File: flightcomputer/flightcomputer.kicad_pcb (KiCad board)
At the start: 4 copper layers, 100 x 75 mm, 65 parts, among them J1 Conn_Coaxial, J10 Conn_01x03, J11 Conn_01x03, J12 ESQ-113-14-G-D, J14 S3B-PH-K-S-GW, J2 Conn_Coaxial, J3 Conn_Coaxial, J4 Conn_Coaxial, J5 S3B-PH-K-S-GW, J6 Conn_01x03, J7 S4B-PH-K-S_LF__SN_, J8 Conn_01x03, J9 Conn_01x06, U1 MAX-M10S, U2 LIS2MDLTR, U3 BMI088, U4 MS5607-02BA, U6 S2P-VH, U7 Teensy4.1, U8 LSM6DSO32TR, U9 RFM96W-433S2

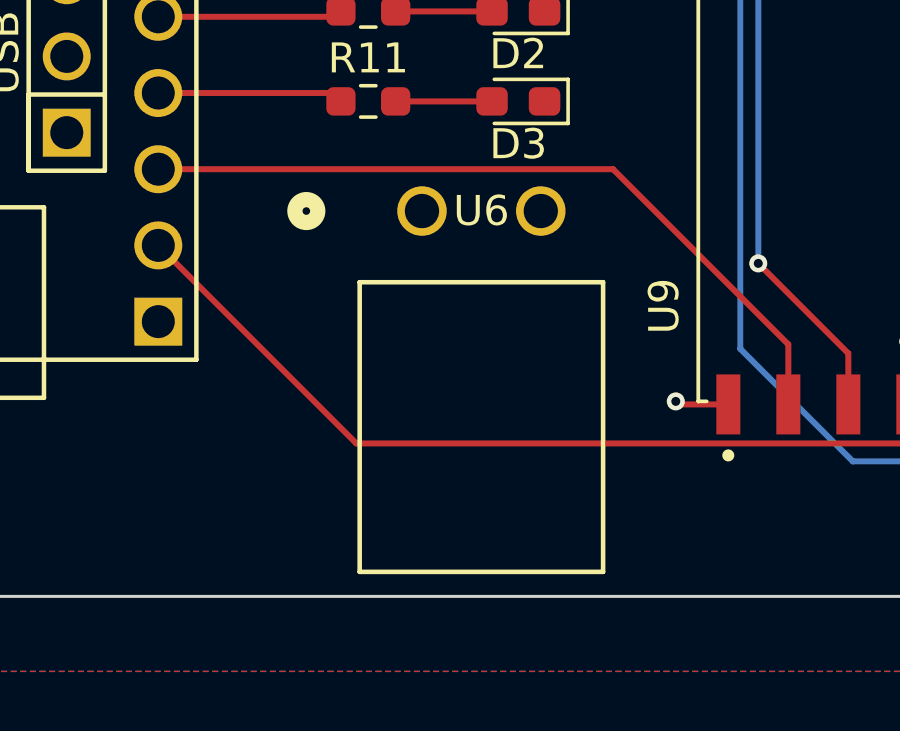
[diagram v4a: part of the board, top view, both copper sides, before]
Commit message: use vert jst
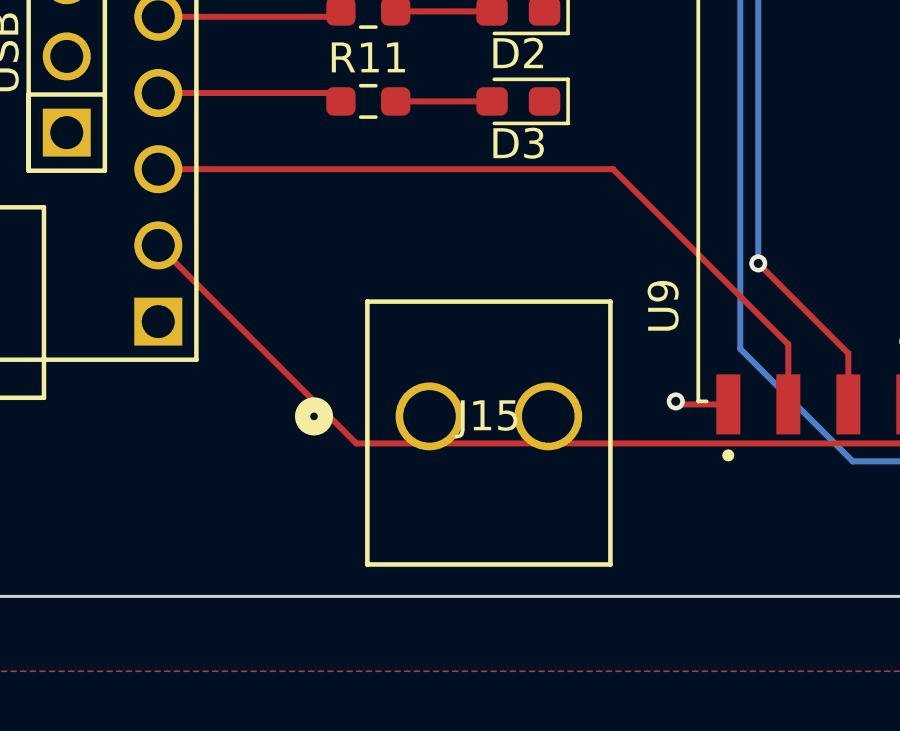
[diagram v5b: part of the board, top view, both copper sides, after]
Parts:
- removed U6: S2P-VH, HPRlibrary:S2P-VH_JST
- added J15: B2P-VHLFSN, HPRlibrary:CONN_B2P-VH_JST, F.Cu at (92.5, 131.5)
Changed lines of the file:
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@@
 		)
 	)
-	(footprint "HPRlibrary:S2P-VH_JST"
-		(layer "F.Cu")
-		(at 92.289999 124.654901)
-		(tags "S2P-VH ")
-		(property "Reference" "U6"
-			(at 1.98 0 0)
-			(unlocked yes)
-			(layer "F.SilkS")
-			(effects
-				(font
-					(size 1 1)
-					(thickness 0.15)
-				)
-			)
-		)
-		(property "Value" "S2P-VH"
-			(at 1.98 0 0)
-			(unlocked yes)
-			(layer "F.Fab")
-			(effects
-				(font
-					(size 1 1)
-					(thickness 0.15)
-				)
-			)
-		)
-		(property "Datasheet" "S2P-VH"
-			(at 0 0 0)
-			(layer "F.Fab")
-			(hide yes)
-			(effects
-				(font
-					(size 1.27 1.27)
-					(thickness 0.15)
-				)
-			)
-		)
-		(property "Description" ""
-			(at 0 0 0)
-			(layer "F.Fab")
-			(hide yes)
-			(effects
-				(font
-					(size 1.27 1.27)
-					(thickness 0.15)
-				)
-			)
-		)
-		(property ki_fp_filters "S2P-VH_JST")
-		(sheetname "/")
-		(sheetfile "flightcomputer.kicad_sch")
-		(attr through_hole)
-		(fp_line
-			(start -2.077 2.373)
-			(end -2.077 12.026999)
-			(stroke
-				(width 0.1524)
-				(type solid)
-			)
-			(layer "F.SilkS")
-		)
-		(fp_line
-			(start -2.077 12.026999)
-			(end 6.037 12.026999)
-			(stroke
-				(width 0.1524)
-				(type solid)
-			)
-			(layer "F.SilkS")
-		)
-		(fp_line
-			(start 6.037 2.373)
-			(end -2.077 2.373)
-			(stroke
-				(width 0.1524)
-				(type solid)
-			)
-			(layer "F.SilkS")
-		)
-		(fp_line
-			(start 6.037 12.026999)
-			(end 6.037 2.373)
-			(stroke
-				(width 0.1524)
-				(type solid)
-			)
-			(layer "F.SilkS")
-		)
-		(fp_circle
-			(center -3.855 0)
-			(end -3.474 0)
-			(stroke
-				(width 0.508)
-				(type solid)
-			)
-			(fill no)
-			(layer "F.SilkS")
-		)
-		(fp_circle
-			(center -3.855 0)
-			(end -3.474 0)
-			(stroke
-				(width 0.508)
-				(type solid)
-			)
-			(fill no)
-			(layer "B.SilkS")
-		)
-		(fp_line
-			(start -2.204 -1.0795)
-			(end -2.204 12.153999)
-			(stroke
-				(width 0.1524)
-				(type solid)
-			)
-			(layer "F.CrtYd")
-		)
-		(fp_line
-			(start -2.204 12.153999)
-			(end 6.164 12.153999)
-			(stroke
-				(width 0.1524)
-				(type solid)
-			)
-			(layer "F.CrtYd")
-		)
-		(fp_line
-			(start 6.164 -1.0795)
-			(end -2.204 -1.0795)
-			(stroke
-				(width 0.1524)
-				(type solid)
-			)
-			(layer "F.CrtYd")
-		)
-		(fp_line
-			(start 6.164 12.153999)
-			(end 6.164 -1.0795)
-			(stroke
-				(width 0.1524)
-				(type solid)
-			)
-			(layer "F.CrtYd")
-		)
-		(fp_line
-			(start -1.95 2.5)
-			(end -1.95 11.899999)
-			(stroke
-				(width 0.0254)
-				(type solid)
-			)
-			(layer "F.Fab")
-		)
-		(fp_line
-			(start -1.95 11.899999)
-			(end 5.91 11.899999)
-			(stroke
-				(width 0.0254)
-				(type solid)
-			)
-			(layer "F.Fab")
-		)
-		(fp_line
-			(start 5.91 2.5)
-			(end -1.95 2.5)
-			(stroke
-				(width 0.0254)
-				(type solid)
-			)
-			(layer "F.Fab")
-		)
-		(fp_line
-			(start 5.91 11.899999)
-			(end 5.91 2.5)
-			(stroke
-				(width 0.0254)
-				(type solid)
-			)
-			(layer "F.Fab")
-		)
-		(fp_circle
-			(center 0 -1.905)
-			(end 0.381 -1.905)
-			(stroke
-				(width 0.508)
-				(type solid)
-			)
-			(fill no)
-			(layer "F.Fab")
-		)
-		(fp_text user "${REFERENCE}"
-			(at 1.98 0 0)
-			(unlocked yes)
-			(layer "F.Fab")
-			(effects
-				(font
-					(size 1 1)
-					(thickness 0.15)
-				)
-			)
-		)
-		(pad "1" thru_hole circle
-			(at 0 0)
-			(size 1.651 1.651)
-			(drill 1.143)
-			(layers "*.Cu" "*.Mask")
-			(remove_unused_layers no)
-			(net 86 "/5V")
-			(pinfunction "1")
-			(pintype "unspecified")
-		)
-		(pad "2" thru_hole circle
-			(at 3.960001 0)
-			(size 1.651 1.651)
-			(drill 1.143)
-			(layers "*.Cu" "*.Mask")
-			(remove_unused_layers no)
-			(net 2 "GND")
-			(pinfunction "2")
-			(pintype "unspecified")
-		)
-		(embedded_fonts no)
-	)
 	(footprint "Connector_PinHeader_2.54mm:PinHeader_1x01_P2.54mm_Vertical"
 		(layer "F.Cu")
@@
 		)
 	)
+	(footprint "HPRlibrary:CONN_B2P-VH_JST"
+		(layer "F.Cu")
+		(at 92.539999 131.5)
+		(tags "B2P-VHLFSN ")
+		(property "Reference" "J15"
+			(at 1.98 0 0)
+			(unlocked yes)
+			(layer "F.SilkS")
+			(effects
+				(font
+					(size 1 1)
+					(thickness 0.15)
+				)
+			)
+		)
+		(property "Value" "B2P-VHLFSN"
+			(at 1.98 0 0)
+			(unlocked yes)
+			(layer "F.Fab")
+			(effects
+				(font
+					(size 1 1)
+					(thickness 0.15)
+				)
+			)
+		)
+		(property "Datasheet" "B2P-VHLFSN"
+			(at 0 0 0)
+			(layer "F.Fab")
+			(hide yes)
+			(effects
+				(font
+					(size 1.27 1.27)
+					(thickness 0.15)
+				)
+			)
+		)
+		(property "Description" ""
+			(at 0 0 0)
+			(layer "F.Fab")
+			(hide yes)
+			(effects
+				(font
+					(size 1.27 1.27)
+					(thickness 0.15)
+				)
+			)
+		)
+		(property ki_fp_filters "CONN_B2P-VH_JST")
+		(sheetname "/")
+		(sheetfile "flightcomputer.kicad_sch")
+		(attr through_hole)
+		(fp_line
+			(start -2.0713 -3.827)
+			(end -2.0713 4.936)
+			(stroke
+				(width 0.1524)
+				(type solid)
+			)
+			(layer "F.SilkS")
+		)
+		(fp_line
+			(start -2.0713 4.936)
+			(end 6.0313 4.936)
+			(stroke
+				(width 0.1524)
+				(type solid)
+			)
+			(layer "F.SilkS")
+		)
+		(fp_line
+			(start 6.0313 -3.827)
+			(end -2.0713 -3.827)
+			(stroke
+				(width 0.1524)
+				(type solid)
+			)
+			(layer "F.SilkS")
+		)
+		(fp_line
+			(start 6.0313 4.936)
+			(end 6.0313 -3.827)
+			(stroke
+				(width 0.1524)
+				(type solid)
+			)
+			(layer "F.SilkS")
+		)
+		(fp_circle
+			(center -3.8493 0)
+			(end -3.4683 0)
+			(stroke
+				(width 0.508)
+				(type solid)
+			)
+			(fill no)
+			(layer "F.SilkS")
+		)
+		(fp_circle
+			(center -3.8493 0)
+			(end -3.4683 0)
+			(stroke
+				(width 0.508)
+				(type solid)
+			)
+			(fill no)
+			(layer "B.SilkS")
+		)
+		(fp_line
+			(start -2.1983 -3.954)
+			(end -2.1983 5.063)
+			(stroke
+				(width 0.1524)
+				(type solid)
+			)
+			(layer "F.CrtYd")
+		)
+		(fp_line
+			(start -2.1983 5.063)
+			(end 6.1583 5.063)
+			(stroke
+				(width 0.1524)
+				(type solid)
+			)
+			(layer "F.CrtYd")
+		)
+		(fp_line
+			(start 6.1583 -3.954)
+			(end -2.1983 -3.954)
+			(stroke
+				(width 0.1524)
+				(type solid)
+			)
+			(layer "F.CrtYd")
+		)
+		(fp_line
+			(start 6.1583 5.063)
+			(end 6.1583 -3.954)
+			(stroke
+				(width 0.1524)
+				(type solid)
+			)
+			(layer "F.CrtYd")
+		)
+		(fp_line
+			(start -1.9443 -3.7)
+			(end -1.9443 4.809)
+			(stroke
+				(width 0.0254)
+				(type solid)
+			)
+			(layer "F.Fab")
+		)
+		(fp_line
+			(start -1.9443 4.809)
+			(end 5.9043 4.809)
+			(stroke
+				(width 0.0254)
+				(type solid)
+			)
+			(layer "F.Fab")
+		)
+		(fp_line
+			(start 5.9043 -3.7)
+			(end -1.9443 -3.7)
+			(stroke
+				(width 0.0254)
+				(type solid)
+			)
+			(layer "F.Fab")
+		)
+		(fp_line
+			(start 5.9043 4.809)
+			(end 5.9043 -3.7)
+			(stroke
+				(width 0.0254)
+				(type solid)
+			)
+			(layer "F.Fab")
+		)
+		(fp_circle
+			(center 0 -1.905)
+			(end 0.381 -1.905)
+			(stroke
+				(width 0.508)
+				(type solid)
+			)
+			(fill no)
+			(layer "F.Fab")
+		)
+		(fp_text user "${REFERENCE}"
+			(at 1.98 0 0)
+			(unlocked yes)
+			(layer "F.Fab")
+			(effects
+				(font
+					(size 1 1)
+					(thickness 0.15)
+				)
+			)
+		)
+		(pad "1" thru_hole circle
+			(at 0 0)
+			(size 2.2606 2.2606)
+			(drill 1.7526)
+			(layers "*.Cu" "*.Mask")
+			(remove_unused_layers no)
+			(net 86 "/5V")
+			(pinfunction "1")
+			(pintype "unspecified")
+		)
+		(pad "2" thru_hole circle
+			(at 3.960001 0)
+			(size 2.2606 2.2606)
+			(drill 1.7526)
+			(layers "*.Cu" "*.Mask")
+			(remove_unused_layers no)
+			(net 2 "GND")
+			(pinfunction "2")
+			(pintype "unspecified")
+		)
+		(embedded_fonts no)
+	)
 	(footprint "MountingHole:MountingHole_2.2mm_M2_DIN965_Pad"

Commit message: add LDO fc
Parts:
- added C11: 1uF, Capacitor_SMD:C_0603_1608Metric_Pad1.08x0.95mm_HandSolder, F.Cu at (88.8, 122.5)
- added C12: 1uF, Capacitor_SMD:C_0603_1608Metric_Pad1.08x0.95mm_HandSolder, F.Cu at (96.0, 123.2)
- added R16: 31.6k, Resistor_SMD:R_0603_1608Metric_Pad0.98x0.95mm_HandSolder, F.Cu at (92.8, 125.8)
- added R18: 10k, Resistor_SMD:R_0603_1608Metric_Pad0.98x0.95mm_HandSolder, F.Cu at (88.8, 125.8)
- added R19: 0, Resistor_SMD:R_0603_1608Metric_Pad0.98x0.95mm_HandSolder, F.Cu at (96.2, 126.0)
- added U6: NCP718ASNADJT1G, HPRlibrary:TSOT-23-5_2P9X1P6_ONS-L, F.Cu at (92.3, 123.0)
- moved D3 1.51 mm to (95.4, 119.5)
- moved R11 1.51 mm to (90.4, 119.5)
- moved R10 0.76 mm to (90.4, 117.2)
- moved D2 0.75 mm to (95.5, 117.2)
- moved J15 0.20 mm to (92.5, 131.7)
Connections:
- J15 pad 1: /5V -> /V_ext
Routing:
- net /LDO_5V: track 0.00 -> 6.77 mm
- net Net-(U6-NC/ADJ): track 0.00 -> 4.71 mm
- net /V_ext: track 0.00 -> 1.88 mm, vias 0 -> 3
- net /radio_miso: track 25.4 -> 27.3 mm
- net /radio_cs: track 30.3 -> 31.4 mm
- net /LED3: track 6.20 -> 6.86 mm
- net GND: vias 20 -> 24
- net /5V: vias 0 -> 1

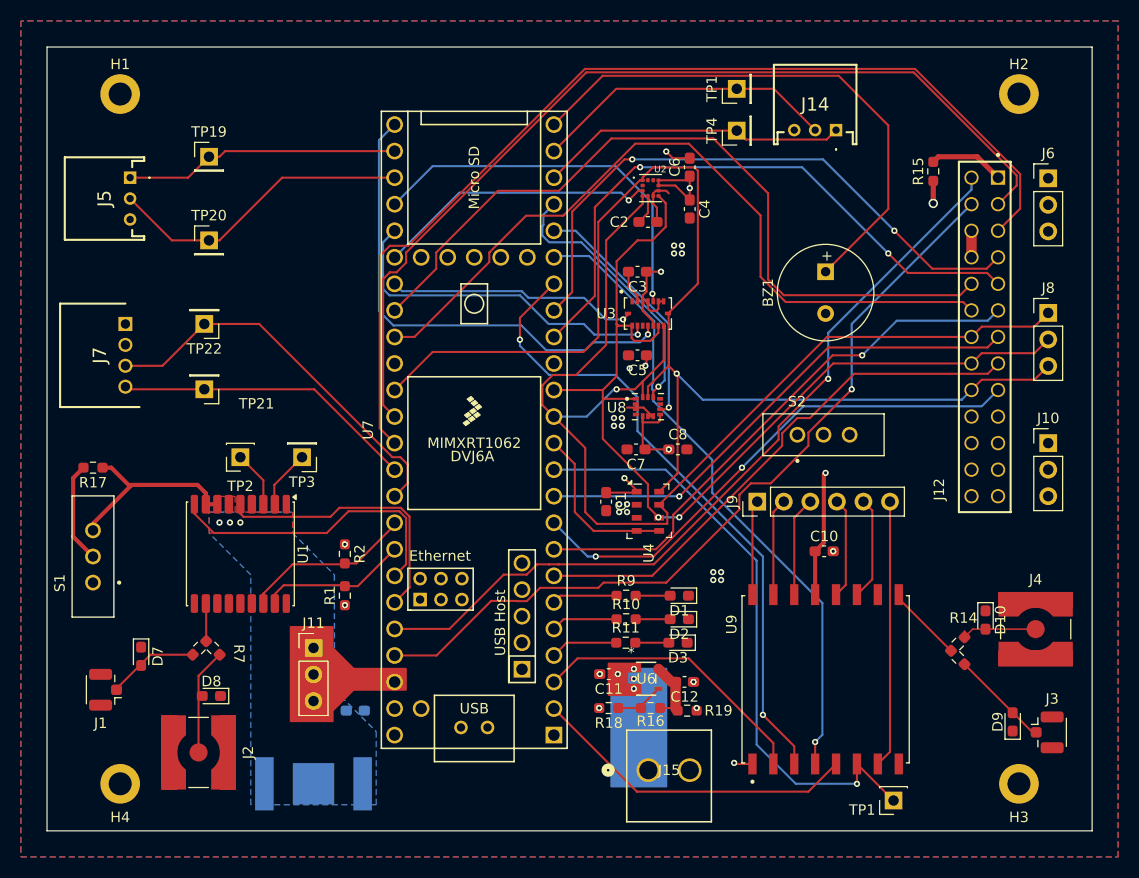
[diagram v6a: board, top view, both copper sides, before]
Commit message: add on/off test pad
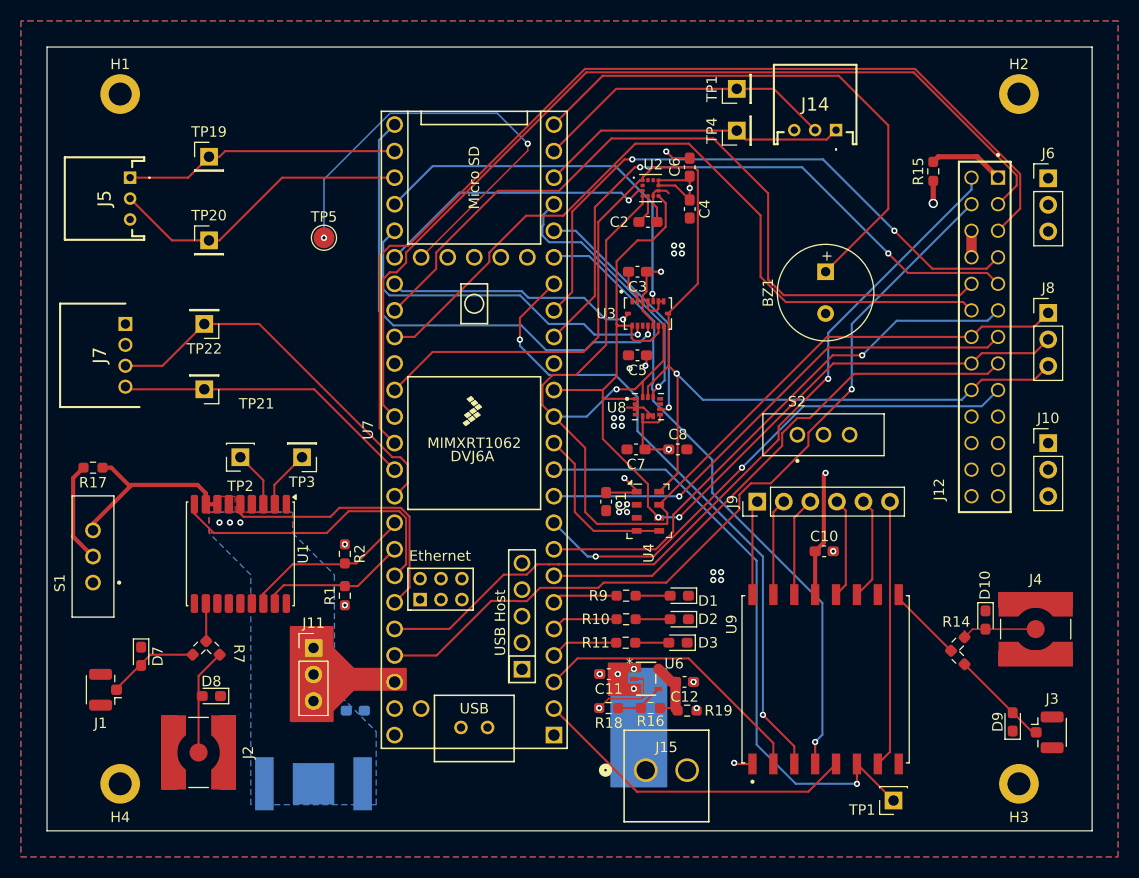
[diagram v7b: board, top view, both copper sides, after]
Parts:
- added TP5: TestPoint, TestPoint:TestPoint_Pad_D2.0mm, F.Cu at (61.5, 80.8)
- moved J15 0.25 mm to (92.3, 131.7)
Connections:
- U7 pad 54: unconnected-(U7-ON_OFF-Pad54) -> Net-(U7-ON_OFF)
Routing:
- net Net-(U7-ON_OFF): track 0.00 -> 44.2 mm, vias 0 -> 2
- net GND: track 18.8 -> 26.1 mm, vias 24 -> 23
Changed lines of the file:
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@@
 	(net 72 "unconnected-(U1-TIMEPULSE-Pad4)")
 	(net 73 "unconnected-(U1-VIO_SEL-Pad15)")
-	(net 74 "unconnected-(U7-ON_OFF-Pad54)")
+	(net 74 "Net-(U7-ON_OFF)")
 	(net 75 "/servo2_pwm")
 	(net 76 "unconnected-(U7-GND-Pad58)")
@@
 		(tags "LED handsolder")
 		(property "Reference" "D1"
-			(at 0 -1.43 0)
+			(at -2.75 -0.5 0)
 			(layer "F.SilkS")
 			(effects
@@
 		(tags "resistor handsolder")
 		(property "Reference" "R11"
-			(at 0 -1.43 0)
+			(at -2.875 0 0)
 			(layer "F.SilkS")
 			(effects
@@
 		(at 122.690917 117.628649)
 		(property "Reference" "R14"
-			(at 0 -0.5 0)
+			(at -0.690917 -0.128649 0)
 			(unlocked yes)
 			(layer "F.SilkS")
@@
 		(tags "NCP718ASNADJT1G ")
 		(property "Reference" "U6"
-			(at 0 0 0)
+			(at 2.67475 -1.450001 0)
 			(unlocked yes)
 			(layer "F.SilkS")
@@
 		)
 		(fp_text user "*"
-			(at -1.42875 -2.4994 0)
-			(unlocked yes)
-			(layer "F.SilkS")
-			(effects
-				(font
-					(size 1 1)
-					(thickness 0.15)
-				)
-			)
-		)
-		(fp_text user "*"
-			(at -1.42875 -2.4994 0)
+			(at -1.57525 -1.450001 0)
 			(layer "F.SilkS")
 			(effects
@@
 		(tags "LED handsolder")
 		(property "Reference" "D3"
-			(at 0 -1.43 0)
+			(at -2.875 0 0)
 			(layer "F.SilkS")
 			(effects
@@
 		(tags "resistor handsolder")
 		(property "Reference" "R9"
-			(at 0 -1.43 0)
+			(at -2.6625 0 0)
 			(layer "F.SilkS")
 			(effects
@@
 		(tags "resistor handsolder")
 		(property "Reference" "R10"
-			(at 0 -1.43 0)
+			(at -2.9125 0 0)
 			(layer "F.SilkS")
 			(effects
@@
 		(tags "diode handsolder")
 		(property "Reference" "D10"
-			(at 0 -1.43 270)
+			(at -3.325 0.05 270)
 			(layer "F.SilkS")
 			(effects
@@
 		(at 92.75 76)
 		(property "Reference" "U2"
-			(at 0.932 -1.8064 0)
+			(at 0.25 -2.25 0)
 			(layer "F.SilkS")
 			(effects
 				(font
-					(size 0.64 0.64)
+					(size 1 1)
 					(thickness 0.15)
 				)
@@
 	(footprint "HPRlibrary:CONN_B2P-VH_JST"
 		(layer "F.Cu")
-		(at 92.539999 131.6955)
+		(at 92.289999 131.6955)
 		(tags "B2P-VHLFSN ")
 		(property "Reference" "J15"
-			(at 1.98 0 0)
+			(at 1.98 -2.1955 0)
 			(unlocked yes)
 			(layer "F.SilkS")
@@
 			(layers "*.Cu" "*.Mask")
 			(remove_unused_layers no)
-			(net 74 "unconnected-(U7-ON_OFF-Pad54)")
+			(net 74 "Net-(U7-ON_OFF)")
 			(pinfunction "ON_OFF")
 			(pintype "input")
@@
 		(tags "LED handsolder")
 		(property "Reference" "D2"
-			(at 0 -1.43 0)
+			(at -2.75 0 0)
 			(layer "F.SilkS")
 			(effects
@@
 		)
 	)
+	(footprint "TestPoint:TestPoint_Pad_D2.0mm"
+		(layer "F.Cu")
+		(at 61.5 80.75)
+		(descr "SMD pad as test Point, diameter 2.0mm")
+		(tags "test point SMD pad")
+		(property "Reference" "TP5"
+			(at 0 -1.998 0)
+			(layer "F.SilkS")
+			(effects
+				(font
+					(size 1 1)
+					(thickness 0.15)
+				)
+			)
+		)
+		(property "Value" "TestPoint"
+			(at 0 2.05 0)
+			(layer "F.Fab")
+			(effects
+				(font
+					(size 1 1)
+					(thickness 0.15)
+				)
+			)
+		)
+		(property "Datasheet" "~"
+			(at 0 0 0)
+			(unlocked yes)
+			(layer "F.Fab")
+			(hide yes)
+			(effects
+				(font
+					(size 1.27 1.27)
+					(thickness 0.15)
+				)
+			)
+		)
+		(property "Description" "test point"
+			(at 0 0 0)
+			(unlocked yes)
+			(layer "F.Fab")
+			(hide yes)
+			(effects
+				(font
+					(size 1.27 1.27)
+					(thickness 0.15)
+				)
+			)
+		)
+		(property ki_fp_filters "Pin* Test*")
+		(sheetname "/")
+		(sheetfile "flightcomputer.kicad_sch")
+		(attr exclude_from_pos_files)
+		(fp_circle
+			(center 0 0)
+			(end 0 1.2)
+			(stroke
+				(width 0.12)
+				(type solid)
+			)
+			(fill no)
+			(layer "F.SilkS")
+		)
+		(fp_circle
+			(center 0 0)
+			(end 1.5 0)
+			(stroke
+				(width 0.05)
+				(type solid)
+			)
+			(fill no)
+			(layer "F.CrtYd")
+		)
+		(fp_text user "${REFERENCE}"
+			(at 0 -2 0)
+			(layer "F.Fab")
+			(effects
+				(font
+					(size 1 1)
+					(thickness 0.15)
+				)
+			)
+		)
+		(pad "1" smd circle
+			(at 0 0)
+			(size 2 2)
+			(layers "F.Cu" "F.Mask")
+			(net 74 "Net-(U7-ON_OFF)")
+			(pinfunction "1")
+			(pintype "passive")
+		)
+		(embedded_fonts no)
+	)
 	(footprint "HPRlibrary:SW_EG1218"
 		(layer "F.Cu")
@@
 	)
 	(segment
+		(start 91.976 122.950001)
+		(end 91.1505 122.950001)
+		(width 0.15)
+		(layer "F.Cu")
+		(net 2)
+	)
+	(segment
+		(start 92.076 124.635034)
+		(end 92.076 123.050001)
+		(width 0.15)
+		(layer "F.Cu")
+		(net 2)
+	)
+	(segment
+		(start 88.7615 124.826)
+		(end 91.885034 124.826)
+		(width 0.15)
+		(layer "F.Cu")
+		(net 2)
+	)
+	(segment
 		(start 91.3375 96.6625)
 		(end 91.3375 97)
@@
 	)
 	(segment
+		(start 92.076 123.050001)
+		(end 91.976 122.950001)
+		(width 0.15)
+		(layer "F.Cu")
+		(net 2)
+	)
+	(segment
 		(start 92.75 97.825)
 		(end 92.5 97.825)
@@
 	)
 	(segment
+		(start 87.8375 125.75)
+		(end 88.7615 124.826)
+		(width 0.15)
+		(layer "F.Cu")
+		(net 2)
+	)
+	(segment
 		(start 92.75 87.75)
 		(end 93.3035 87.75)
@@
 	)
 	(segment
+		(start 91.885034 124.826)
+		(end 92.076 124.635034)
+		(width 0.15)
+		(layer "F.Cu")
+		(net 2)
+	)
+	(segment
 		(start 93.5 87.5535)
 		(end 93.5 86.835)
@@
 	)
 	(via
-		(at 91.1505 122.950001)
-		(size 0.6)
-		(drill 0.3)
-		(layers "F.Cu" "B.Cu")
-		(net 2)
-	)
-	(via
 		(at 90 98)
 		(size 0.6)
@@
 	)
 	(segment
+		(start 70.8 82.62)
+		(end 70.8 82.45)
+		(width 0.15)
+		(layer "F.Cu")
+		(net 74)
+	)
+	(segment
+		(start 81 72.42)
+		(end 81 71.75)
+		(width 0.15)
+		(layer "F.Cu")
+		(net 74)
+	)
+	(segment
+		(start 70.8 82.62)
+		(end 81 72.42)
+		(width 0.15)
+		(layer "F.Cu")
+		(net 74)
+	)
+	(via
+		(at 61.5 80.75)
+		(size 0.6)
+		(drill 0.3)
+		(layers "F.Cu" "B.Cu")
+		(net 74)
+	)
+	(via
+		(at 81 71.75)
+		(size 0.6)
+		(drill 0.3)
+		(layers "F.Cu" "B.Cu")
+		(net 74)
+	)
+	(segment
+		(start 67.814306 68.844)
+		(end 61.5 75.158306)
+		(width 0.15)
+		(layer "B.Cu")
+		(net 74)
+	)
+	(segment
+		(start 78.094 68.844)
+		(end 67.814306 68.844)
+		(width 0.15)
+		(layer "B.Cu")
+		(net 74)
+	)
+	(segment
+		(start 61.5 75.158306)
+		(end 61.5 80.75)
+		(width 0.15)
+		(layer "B.Cu")
+		(net 74)
+	)
+	(segment
+		(start 81 71.75)
+		(end 78.094 68.844)
+		(width 0.15)
+		(layer "B.Cu")
+		(net 74)
+	)
+	(segment
